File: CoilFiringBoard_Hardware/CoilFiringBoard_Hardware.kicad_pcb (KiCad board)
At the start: 2 copper layers, 101.6 x 76.2 mm, 19 parts, among them Q1 Q_NMOS_GDS, Q2 Q_NMOS_GDS

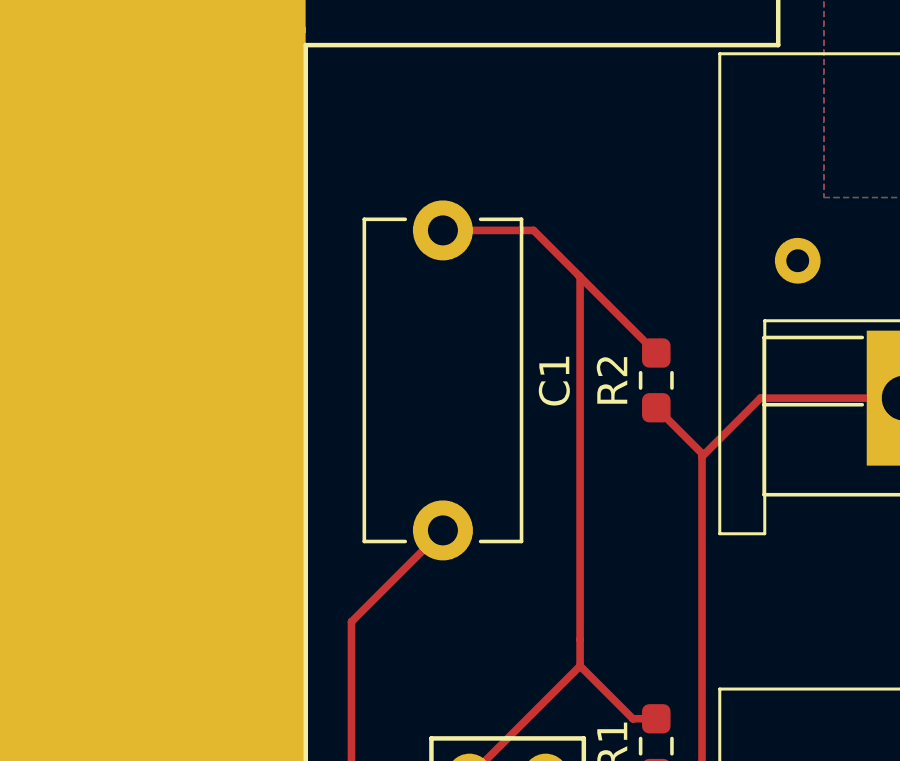
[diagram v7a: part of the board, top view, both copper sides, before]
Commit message: Changed cap footprint
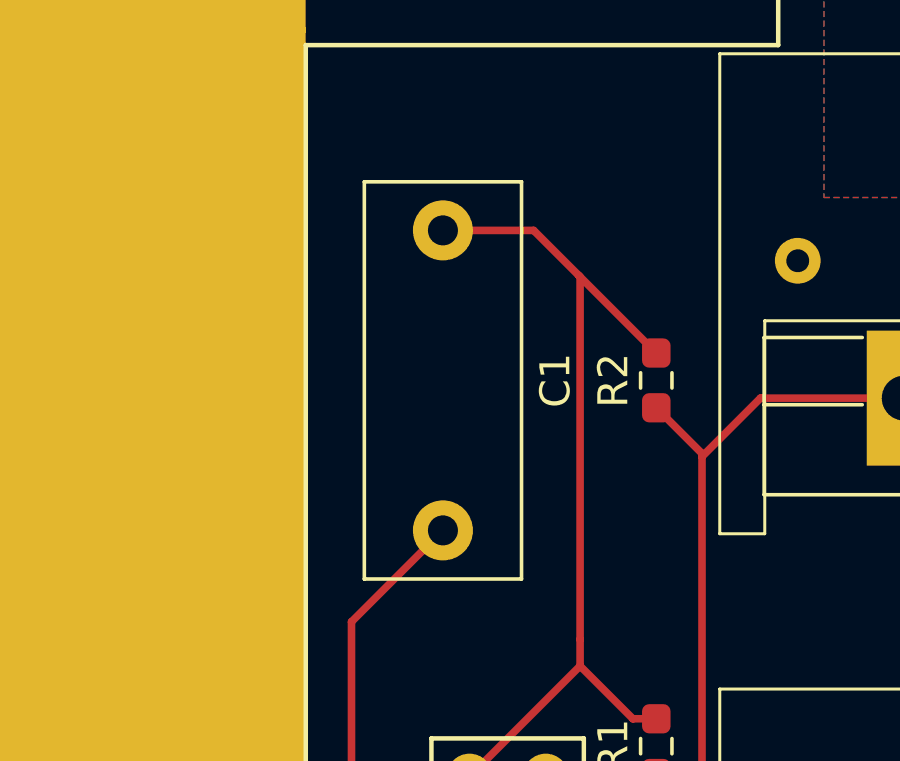
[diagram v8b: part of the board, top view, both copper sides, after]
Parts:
- C1: footprint Capacitor_THT:C_Disc_D10.5mm_W5.0mm_P10.00mm -> Capacitor_THT:C_Rect_L13.0mm_W5.0mm_P10.00mm_FKS3_FKP3_MKS4
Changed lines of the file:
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@@
       (net 3 "PWR") (pintype "input") (zone_connect 2))
   )
-  (footprint "Capacitor_THT:C_Disc_D10.5mm_W5.0mm_P10.00mm" (layer "F.Cu")
+  (footprint "Capacitor_THT:C_Rect_L13.0mm_W5.0mm_P10.00mm_FKS3_FKP3_MKS4" (layer "F.Cu")
     (at 93.472 83.392 -90)
-    (descr "C, Disc series, Radial, pin pitch=10.00mm, , diameter*width=10.5*5.0mm^2, Capacitor, http://www.vishay.com/docs/28535/vy2series.pdf")
-    (tags "C Disc series Radial pin pitch 10.00mm  diameter 10.5mm width 5.0mm Capacitor")
+    (descr "C, Rect series, Radial, pin pitch=10.00mm, , length*width=13*5mm^2, Capacitor, http://www.wima.com/EN/WIMA_FKS_3.pdf, http://www.wima.com/EN/WIMA_MKS_4.pdf")
+    (tags "C Rect series Radial pin pitch 10.00mm  length 13mm width 5mm Capacitor")
     (property "Sheetfile" "CoilFiringBoard_Hardware.kicad_sch")
     (property "Sheetname" "")
@@
     (property "ki_keywords" "cap capacitor")
     (attr through_hole)
-    (fp_text reference "C1" (at 5 -3.75 90) (layer "F.SilkS")
-        (effects (font (size 1 1) (thickness 0.15)))
-    )
-    (fp_text value "4.7n" (at 5 3.75 90) (layer "F.Fab")
-        (effects (font (size 1 1) (thickness 0.15)))
-    )
-    (fp_text user "${REFERENCE}" (at 5 0 90) (layer "F.Fab")
-        (effects (font (size 1 1) (thickness 0.15)))
-    )
-    (fp_line (start -0.37 -2.62) (end -0.37 -1.256)
-      (stroke (width 0.12) (type solid)) (layer "F.SilkS"))
-    (fp_line (start -0.37 -2.62) (end 10.37 -2.62)
-      (stroke (width 0.12) (type solid)) (layer "F.SilkS"))
-    (fp_line (start -0.37 1.256) (end -0.37 2.62)
-      (stroke (width 0.12) (type solid)) (layer "F.SilkS"))
-    (fp_line (start -0.37 2.62) (end 10.37 2.62)
-      (stroke (width 0.12) (type solid)) (layer "F.SilkS"))
-    (fp_line (start 10.37 -2.62) (end 10.37 -1.256)
-      (stroke (width 0.12) (type solid)) (layer "F.SilkS"))
-    (fp_line (start 10.37 1.256) (end 10.37 2.62)
-      (stroke (width 0.12) (type solid)) (layer "F.SilkS"))
-    (fp_line (start -1.25 -2.75) (end -1.25 2.75)
-      (stroke (width 0.05) (type solid)) (layer "F.CrtYd"))
-    (fp_line (start -1.25 2.75) (end 11.25 2.75)
-      (stroke (width 0.05) (type solid)) (layer "F.CrtYd"))
-    (fp_line (start 11.25 -2.75) (end -1.25 -2.75)
-      (stroke (width 0.05) (type solid)) (layer "F.CrtYd"))
-    (fp_line (start 11.25 2.75) (end 11.25 -2.75)
-      (stroke (width 0.05) (type solid)) (layer "F.CrtYd"))
-    (fp_line (start -0.25 -2.5) (end -0.25 2.5)
-      (stroke (width 0.1) (type solid)) (layer "F.Fab"))
-    (fp_line (start -0.25 2.5) (end 10.25 2.5)
-      (stroke (width 0.1) (type solid)) (layer "F.Fab"))
-    (fp_line (start 10.25 -2.5) (end -0.25 -2.5)
-      (stroke (width 0.1) (type solid)) (layer "F.Fab"))
-    (fp_line (start 10.25 2.5) (end 10.25 -2.5)
+    (fp_text reference "C1" (at 5 -3.75 -90) (layer "F.SilkS")
+        (effects (font (size 1 1) (thickness 0.15)))
+    )
+    (fp_text value "4.7n" (at 5 3.75 -90) (layer "F.Fab")
+        (effects (font (size 1 1) (thickness 0.15)))
+    )
+    (fp_text user "${REFERENCE}" (at 5 0 -90) (layer "F.Fab")
+        (effects (font (size 1 1) (thickness 0.15)))
+    )
+    (fp_line (start -1.62 -2.62) (end -1.62 2.62)
+      (stroke (width 0.12) (type solid)) (layer "F.SilkS"))
+    (fp_line (start -1.62 -2.62) (end 11.62 -2.62)
+      (stroke (width 0.12) (type solid)) (layer "F.SilkS"))
+    (fp_line (start -1.62 2.62) (end 11.62 2.62)
+      (stroke (width 0.12) (type solid)) (layer "F.SilkS"))
+    (fp_line (start 11.62 -2.62) (end 11.62 2.62)
+      (stroke (width 0.12) (type solid)) (layer "F.SilkS"))
+    (fp_line (start -1.75 -2.75) (end -1.75 2.75)
+      (stroke (width 0.05) (type solid)) (layer "F.CrtYd"))
+    (fp_line (start -1.75 2.75) (end 11.75 2.75)
+      (stroke (width 0.05) (type solid)) (layer "F.CrtYd"))
+    (fp_line (start 11.75 -2.75) (end -1.75 -2.75)
+      (stroke (width 0.05) (type solid)) (layer "F.CrtYd"))
+    (fp_line (start 11.75 2.75) (end 11.75 -2.75)
+      (stroke (width 0.05) (type solid)) (layer "F.CrtYd"))
+    (fp_line (start -1.5 -2.5) (end -1.5 2.5)
+      (stroke (width 0.1) (type solid)) (layer "F.Fab"))
+    (fp_line (start -1.5 2.5) (end 11.5 2.5)
+      (stroke (width 0.1) (type solid)) (layer "F.Fab"))
+    (fp_line (start 11.5 -2.5) (end -1.5 -2.5)
+      (stroke (width 0.1) (type solid)) (layer "F.Fab"))
+    (fp_line (start 11.5 2.5) (end 11.5 -2.5)
       (stroke (width 0.1) (type solid)) (layer "F.Fab"))
     (pad "1" thru_hole circle (at 0 0 270) (size 2 2) (drill 1) (layers "*.Cu" "*.Mask")
@@
     (pad "2" thru_hole circle (at 10 0 270) (size 2 2) (drill 1) (layers "*.Cu" "*.Mask")
       (net 4 "GND") (pintype "passive"))
-    (model "${KICAD6_3DMODEL_DIR}/Capacitor_THT.3dshapes/C_Disc_D10.5mm_W5.0mm_P10.00mm.wrl"
+    (model "${KICAD6_3DMODEL_DIR}/Capacitor_THT.3dshapes/C_Rect_L13.0mm_W5.0mm_P10.00mm_FKS3_FKP3_MKS4.wrl"
       (offset (xyz 0 0 0))
       (scale (xyz 1 1 1))
@@
     (style (thickness 0.15) (arrow_length 1.27) (text_position_mode 0) (extension_height 0.58642) (extension_offset 0.5) keep_text_aligned)
   )
+  (segment (start 96.4965 83.392) (end 93.472 83.392) (width 0.254) (layer "F.Cu") (net 1))
   (segment (start 97.99225 84.88775) (end 100.584 87.4795) (width 0.254) (layer "F.Cu") (net 1))
   (segment (start 94.359 101.596) (end 98.044 97.911) (width 0.254) (layer "F.Cu") (net 1))
   (segment (start 97.99225 84.88775) (end 98.044 84.9395) (width 0.254) (layer "F.Cu") (net 1))
-  (segment (start 93.472 83.392) (end 96.4965 83.392) (width 0.254) (layer "F.Cu") (net 1))
   (segment (start 99.8045 99.6715) (end 98.044 97.911) (width 0.254) (layer "F.Cu") (net 1))
   (segment (start 98.044 84.9395) (end 98.044 97.028) (width 0.254) (layer "F.Cu") (net 1))
